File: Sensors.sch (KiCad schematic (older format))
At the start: 11 parts, among them IC801 BME680, U801 MPU-9250

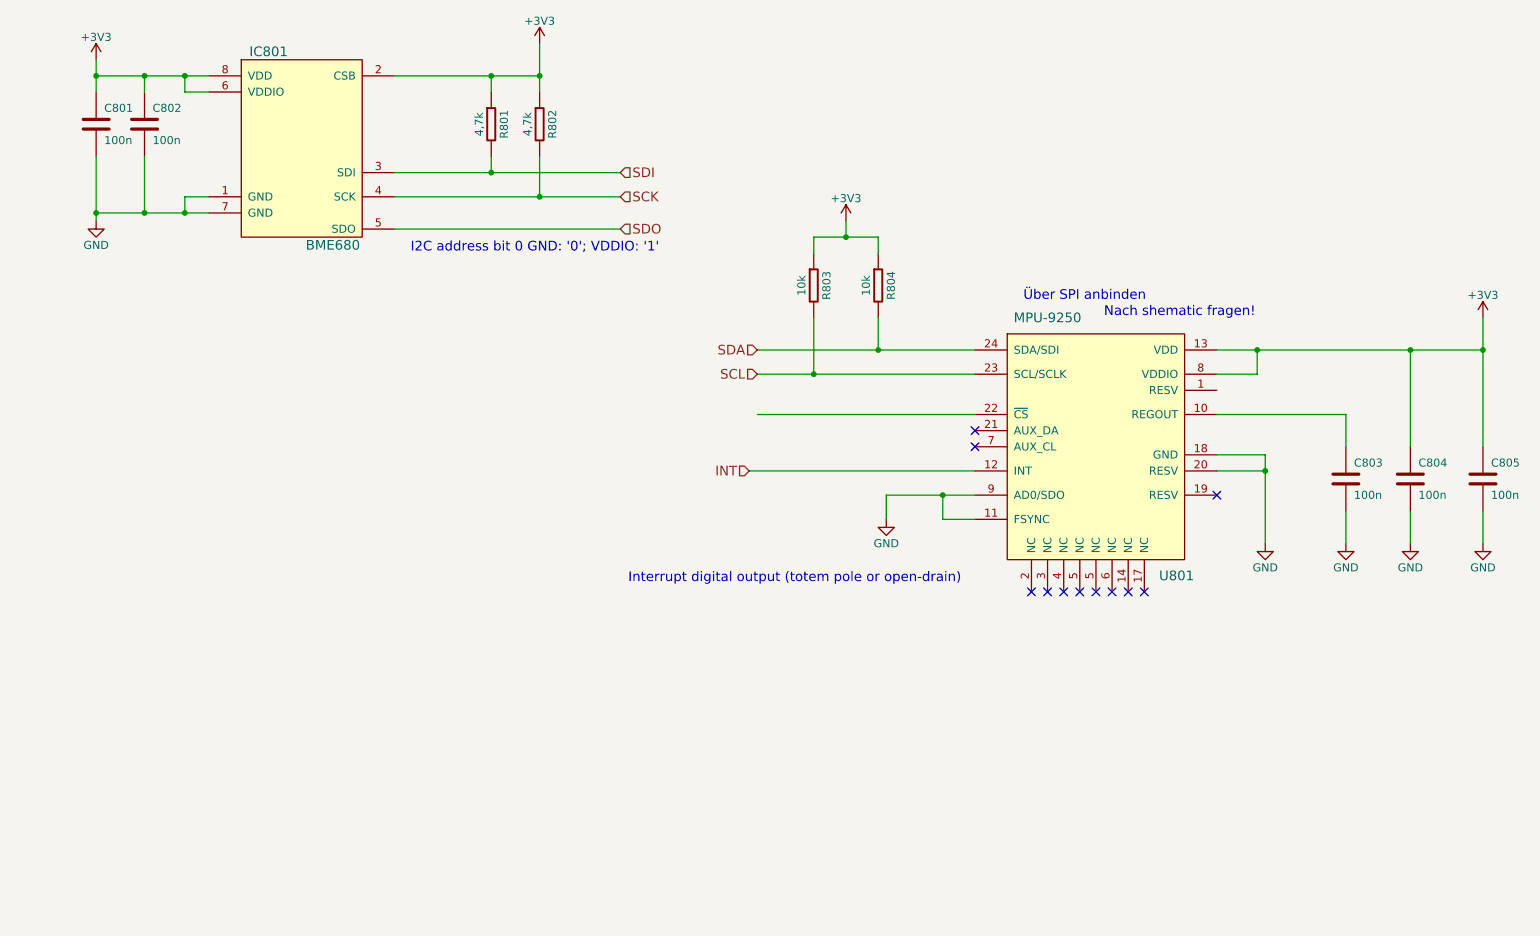
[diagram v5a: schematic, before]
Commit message: adjusted power supply
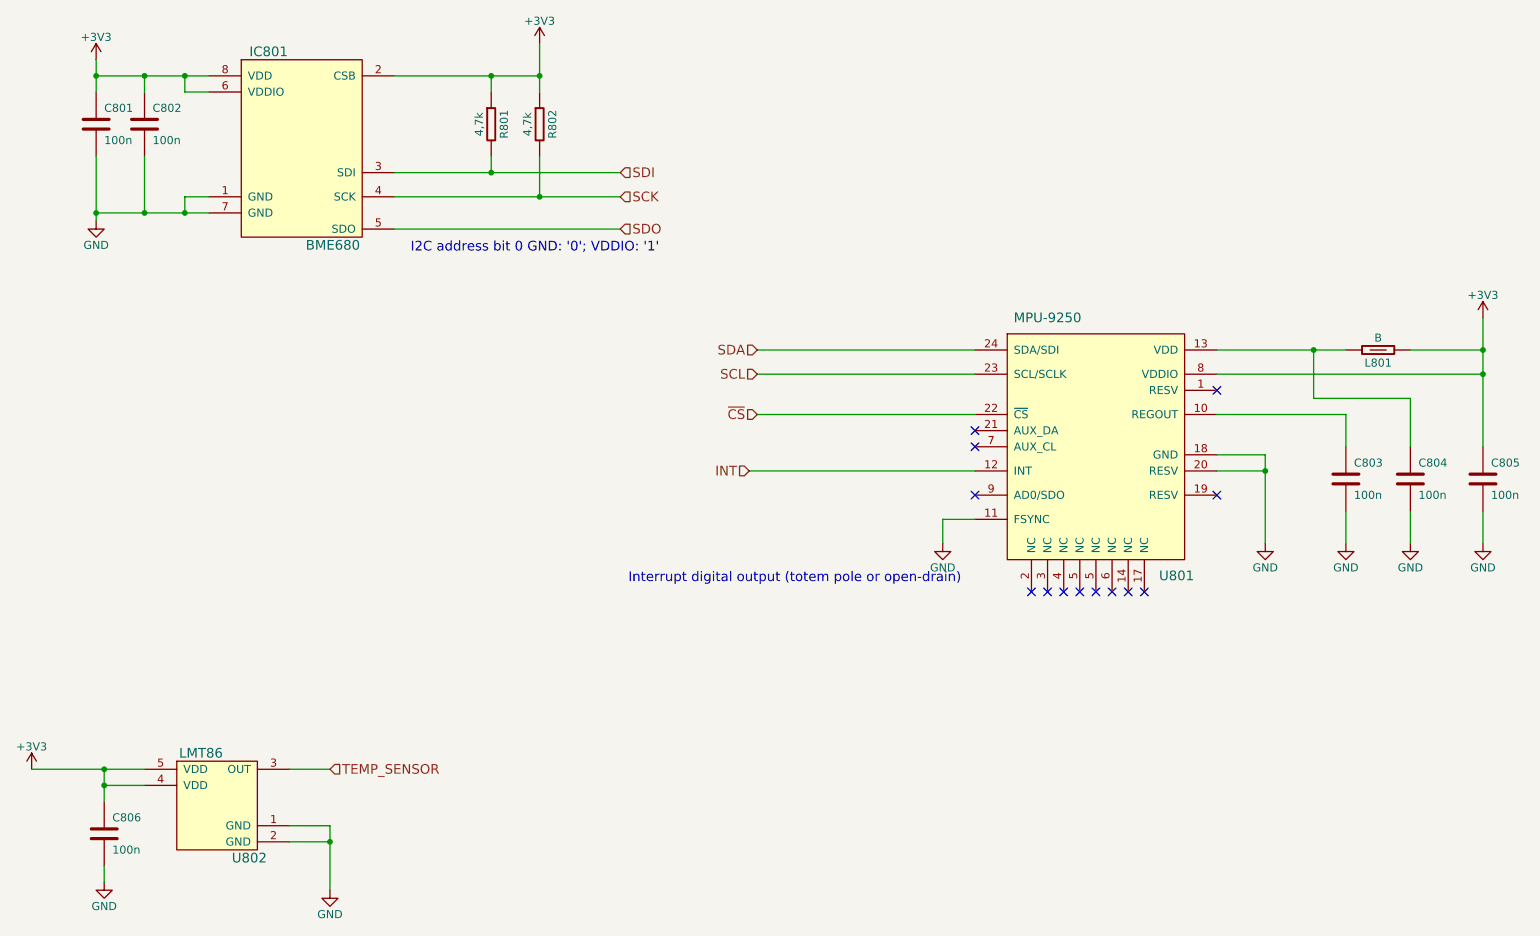
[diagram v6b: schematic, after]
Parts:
- removed R803, R804: 10k, Passives:R0402N, symbol R
- added C806: 100n, Passives:C0402N, symbol C
- added L801: B, symbol B
- added U802: LMT86, symbol LMT86
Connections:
- net +3V3: now also C806.1, L801.1, U802.4 (VDD), U802.5 (VDD); no longer C804.1, U801.13 (VDD)
- net GND: now also C806.2, U802.1 (GND), U802.2 (GND); no longer U801.9 (AD0/SDO)
- net ~CS: now reaches U801.22 (~CS)
- new net: C804.1, L801.2, U801.13 (VDD)
- new net TEMP_SENSOR: U802.3 (OUT)
- no-connect marks 11 -> 13
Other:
- note removed: "Nach shematic fragen!\n"
- note removed: "Über SPI anbinden\n"
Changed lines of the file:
@@
 $EndComp
 $Comp
-L +3V3 #PWR0171
+L +3V3 #PWR802
 U 1 1 5712095D
 P 1450 1000
-F 0 "#PWR0171" H 1450 850 50  0001 C CNN
+F 0 "#PWR802" H 1450 850 50  0001 C CNN
 F 1 "+3V3" H 1450 1140 50  0000 C CNN
 F 2 "" H 1450 1000 50  0000 C CNN
@@
 $EndComp
 $Comp
-L GND #PWR0172
+L GND #PWR803
 U 1 1 5712097D
 P 1450 2000
-F 0 "#PWR0172" H 1450 1750 50  0001 C CNN
+F 0 "#PWR803" H 1450 1750 50  0001 C CNN
 F 1 "GND" H 1450 1850 50  0000 C CNN
 F 2 "" H 1450 2000 50  0000 C CNN
@@
 Wire Wire Line
 	4200 1600 4200 1850
-$Comp
-L R R804
-U 1 1 571216FF
-P 6300 2400
-F 0 "R804" V 6380 2400 50  0000 C CNN
-F 1 "10k" V 6225 2400 50  0000 C CNN
-F 2 "Passives:R0402N" V 6230 2400 30  0001 C CNN
-F 3 "" H 6300 2400 30  0000 C CNN
-	1    6300 2400
-	1    0    0    -1
-$EndComp
 NoConn ~ 7950 4300
 NoConn ~ 7850 4300
@@
 	9200 3200 9200 3400
 $Comp
-L GND #PWR0173
+L GND #PWR808
 U 1 1 57122FCF
 P 8700 4000
-F 0 "#PWR0173" H 8700 3750 50  0001 C CNN
+F 0 "#PWR808" H 8700 3750 50  0001 C CNN
 F 1 "GND" H 8700 3850 50  0000 C CNN
 F 2 "" H 8700 4000 50  0000 C CNN
@@
 $EndComp
 $Comp
-L GND #PWR0174
+L GND #PWR809
 U 1 1 57123008
 P 9200 4000
-F 0 "#PWR0174" H 9200 3750 50  0001 C CNN
+F 0 "#PWR809" H 9200 3750 50  0001 C CNN
 F 1 "GND" H 9200 3850 50  0000 C CNN
 F 2 "" H 9200 4000 50  0000 C CNN
@@
 	9200 3800 9200 4000
 $Comp
-L +3V3 #PWR0175
+L +3V3 #PWR811
 U 1 1 57123302
 P 10050 2600
-F 0 "#PWR0175" H 10050 2450 50  0001 C CNN
+F 0 "#PWR811" H 10050 2450 50  0001 C CNN
 F 1 "+3V3" H 10050 2740 50  0000 C CNN
 F 2 "" H 10050 2600 50  0000 C CNN
@@
 $EndComp
 Wire Wire Line
-	8400 2800 10050 2800
-Wire Wire Line
 	10050 2600 10050 3400
-Wire Wire Line
-	9600 3400 9600 2800
-Connection ~ 9600 2800
 Connection ~ 10050 2800
 Wire Wire Line
-	8400 2950 8650 2950
-Wire Wire Line
-	8650 2950 8650 2800
-Connection ~ 8650 2800
-$Comp
-L GND #PWR0176
+	8400 2950 10050 2950
+$Comp
+L GND #PWR810
 U 1 1 571235AC
 P 9600 4000
-F 0 "#PWR0176" H 9600 3750 50  0001 C CNN
+F 0 "#PWR810" H 9600 3750 50  0001 C CNN
 F 1 "GND" H 9600 3850 50  0000 C CNN
 F 2 "" H 9600 4000 50  0000 C CNN
@@
 $EndComp
 $Comp
-L GND #PWR0177
+L GND #PWR812
 U 1 1 571235FC
 P 10050 4000
-F 0 "#PWR0177" H 10050 3750 50  0001 C CNN
+F 0 "#PWR812" H 10050 3750 50  0001 C CNN
 F 1 "GND" H 10050 3850 50  0000 C CNN
 F 2 "" H 10050 4000 50  0000 C CNN
@@
 Wire Wire Line
 	9600 3800 9600 4000
-$Comp
-L +3V3 #PWR0178
-U 1 1 57127673
-P 6100 2000
-F 0 "#PWR0178" H 6100 1850 50  0001 C CNN
-F 1 "+3V3" H 6100 2140 50  0000 C CNN
-F 2 "" H 6100 2000 50  0000 C CNN
-F 3 "" H 6100 2000 50  0000 C CNN
-	1    6100 2000
-	1    0    0    -1
-$EndComp
 Wire Wire Line
 	6900 2800 5550 2800
 Wire Wire Line
-	6300 2600 6300 2800
-Connection ~ 6300 2800
-Wire Wire Line
 	6900 2950 5550 2950
-Wire Wire Line
-	5900 2600 5900 2950
-Connection ~ 5900 2950
-Wire Wire Line
-	5900 2200 5900 2100
-Wire Wire Line
-	5900 2100 6300 2100
-Wire Wire Line
-	6300 2100 6300 2200
-Wire Wire Line
-	6100 2000 6100 2100
-Connection ~ 6100 2100
 Text HLabel 5550 2800 0    60   Input ~ 0
 SDA
@@
 NoConn ~ 6900 3400
 $Comp
-L GND #PWR0179
+L GND #PWR807
 U 1 1 5712831A
-P 6350 3850
-F 0 "#PWR0179" H 6350 3600 50  0001 C CNN
-F 1 "GND" H 6350 3700 50  0000 C CNN
-F 2 "" H 6350 3850 50  0000 C CNN
-F 3 "" H 6350 3850 50  0000 C CNN
-	1    6350 3850
-	1    0    0    -1
-$EndComp
-Wire Wire Line
-	6350 3850 6350 3700
-Wire Wire Line
-	6350 3700 6900 3700
-Wire Wire Line
-	6900 3850 6700 3850
-Wire Wire Line
-	6700 3850 6700 3700
-Connection ~ 6700 3700
+P 6700 4000
+F 0 "#PWR807" H 6700 3750 50  0001 C CNN
+F 1 "GND" H 6700 3850 50  0000 C CNN
+F 2 "" H 6700 4000 50  0000 C CNN
+F 3 "" H 6700 4000 50  0000 C CNN
+	1    6700 4000
+	1    0    0    -1
+$EndComp
+Wire Wire Line
+	6700 4000 6700 3850
+Wire Wire Line
+	6700 3850 6900 3850
 Text HLabel 5500 3550 0    60   Input ~ 0
 INT
@@
 Connection ~ 3900 1100
 $Comp
-L +3V3 #PWR0180
+L +3V3 #PWR806
 U 1 1 57110B2A
 P 4200 900
-F 0 "#PWR0180" H 4200 750 50  0001 C CNN
+F 0 "#PWR806" H 4200 750 50  0001 C CNN
 F 1 "+3V3" H 4200 1040 50  0000 C CNN
 F 2 "" H 4200 900 50  0000 C CNN
@@
 SDO
 $Comp
-L R R803
-U 1 1 57116F68
-P 5900 2400
-F 0 "R803" V 5980 2400 50  0000 C CNN
-F 1 "10k" V 5825 2400 50  0000 C CNN
-F 2 "Passives:R0402N" V 5830 2400 30  0001 C CNN
-F 3 "" H 5900 2400 30  0000 C CNN
-	1    5900 2400
-	1    0    0    -1
-$EndComp
-$Comp
 L C C804
 U 1 1 57117060
@@
 	1    0    0    -1
 $EndComp
-Text Notes 7200 2500 0    60   ~ 0
-Über SPI anbinden\n
 Wire Wire Line
 	6900 3200 5550 3200
-Text Notes 7700 2600 0    60   ~ 0
-Nach shematic fragen!\n
+$Comp
+L B L801
+U 1 1 5728CE8C
+P 9400 2800
+F 0 "L801" V 9480 2800 50  0000 C CNN
+F 1 "B" V 9325 2800 50  0000 C CNN
+F 2 "" V 9330 2800 30  0001 C CNN
+F 3 "" H 9400 2800 30  0000 C CNN
+	1    9400 2800
+	0    1    1    0
+$EndComp
+Connection ~ 10050 2950
+Wire Wire Line
+	8400 2800 9200 2800
+Wire Wire Line
+	9600 2800 10050 2800
+Wire Wire Line
+	9600 3400 9600 3100
+Wire Wire Line
+	9600 3100 9000 3100
+Wire Wire Line
+	9000 3100 9000 2800
+Connection ~ 9000 2800
+Text HLabel 5550 3200 0    60   Input ~ 0
+~CS
+NoConn ~ 6900 3700
+NoConn ~ 8400 3050
+$Comp
+L LMT86 U802
+U 1 1 57293532
+P 2200 5600
+F 0 "U802" H 2400 5250 60  0000 C CNN
+F 1 "LMT86" H 2100 5900 60  0000 C CNN
+F 2 "" H 2700 5300 60  0000 C CNN
+F 3 "" H 2700 5300 60  0000 C CNN
+	1    2200 5600
+	1    0    0    -1
+$EndComp
+Wire Wire Line
+	1750 5400 1050 5400
+Wire Wire Line
+	1500 5400 1500 5600
+Wire Wire Line
+	1500 5500 1750 5500
+Connection ~ 1500 5400
+Wire Wire Line
+	2650 5750 2900 5750
+Wire Wire Line
+	2900 5750 2900 6150
+Wire Wire Line
+	2650 5850 2900 5850
+Connection ~ 2900 5850
+Wire Wire Line
+	2650 5400 2900 5400
+$Comp
+L GND #PWR805
+U 1 1 572937FC
+P 2900 6150
+F 0 "#PWR805" H 2900 5900 50  0001 C CNN
+F 1 "GND" H 2900 6000 50  0000 C CNN
+F 2 "" H 2900 6150 50  0000 C CNN
+F 3 "" H 2900 6150 50  0000 C CNN
+	1    2900 6150
+	1    0    0    -1
+$EndComp
+$Comp
+L +3V3 #PWR801
+U 1 1 57293831
+P 1050 5400
+F 0 "#PWR801" H 1050 5250 50  0001 C CNN
+F 1 "+3V3" H 1050 5540 50  0000 C CNN
+F 2 "" H 1050 5400 50  0000 C CNN
+F 3 "" H 1050 5400 50  0000 C CNN
+	1    1050 5400
+	1    0    0    -1
+$EndComp
+Text HLabel 2900 5400 2    60   Input ~ 0
+TEMP_SENSOR
+$Comp
+L C C806
+U 1 1 57293999
+P 1500 5800
+F 0 "C806" H 1550 5900 50  0000 L CNN
+F 1 "100n" H 1550 5700 50  0000 L CNN
+F 2 "Passives:C0402N" H 1538 5650 30  0001 C CNN
+F 3 "" H 1550 5900 60  0000 C CNN
+	1    1500 5800
+	1    0    0    -1
+$EndComp
+$Comp
+L GND #PWR804
+U 1 1 57293A10
+P 1500 6100
+F 0 "#PWR804" H 1500 5850 50  0001 C CNN
+F 1 "GND" H 1500 5950 50  0000 C CNN
+F 2 "" H 1500 6100 50  0000 C CNN
+F 3 "" H 1500 6100 50  0000 C CNN
+	1    1500 6100
+	1    0    0    -1
+$EndComp
+Connection ~ 1500 5500
+Wire Wire Line
+	1500 6000 1500 6100
 $EndSCHEMATC

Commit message: adjusted power supply and sensors
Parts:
- L801: footprint (none) -> Passives:B0402N
- U802: footprint (none) -> Sensors:R-PDSO-G5
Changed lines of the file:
@@
 F 0 "L801" V 9480 2800 50  0000 C CNN
 F 1 "B" V 9325 2800 50  0000 C CNN
-F 2 "" V 9330 2800 30  0001 C CNN
+F 2 "Passives:B0402N" V 9330 2800 30  0001 C CNN
 F 3 "" H 9400 2800 30  0000 C CNN
 	1    9400 2800
@@
 F 0 "U802" H 2400 5250 60  0000 C CNN
 F 1 "LMT86" H 2100 5900 60  0000 C CNN
-F 2 "" H 2700 5300 60  0000 C CNN
+F 2 "Sensors:R-PDSO-G5" H 2700 5300 60  0001 C CNN
 F 3 "" H 2700 5300 60  0000 C CNN
 	1    2200 5600
